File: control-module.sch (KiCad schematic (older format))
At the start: 19 parts

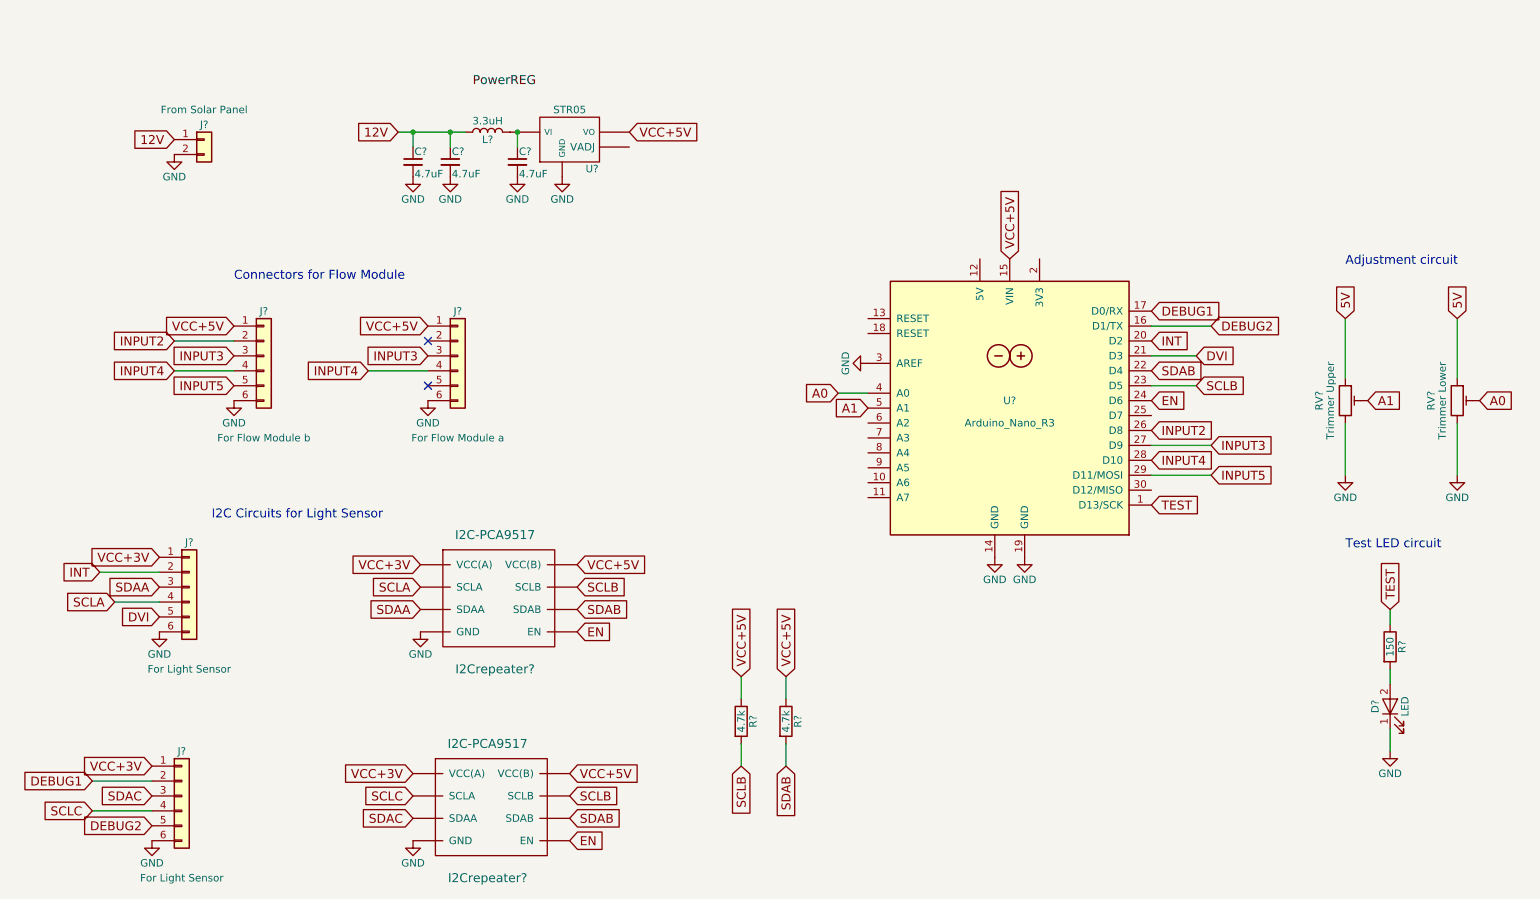
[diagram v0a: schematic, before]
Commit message: PCB Layout for Control Module
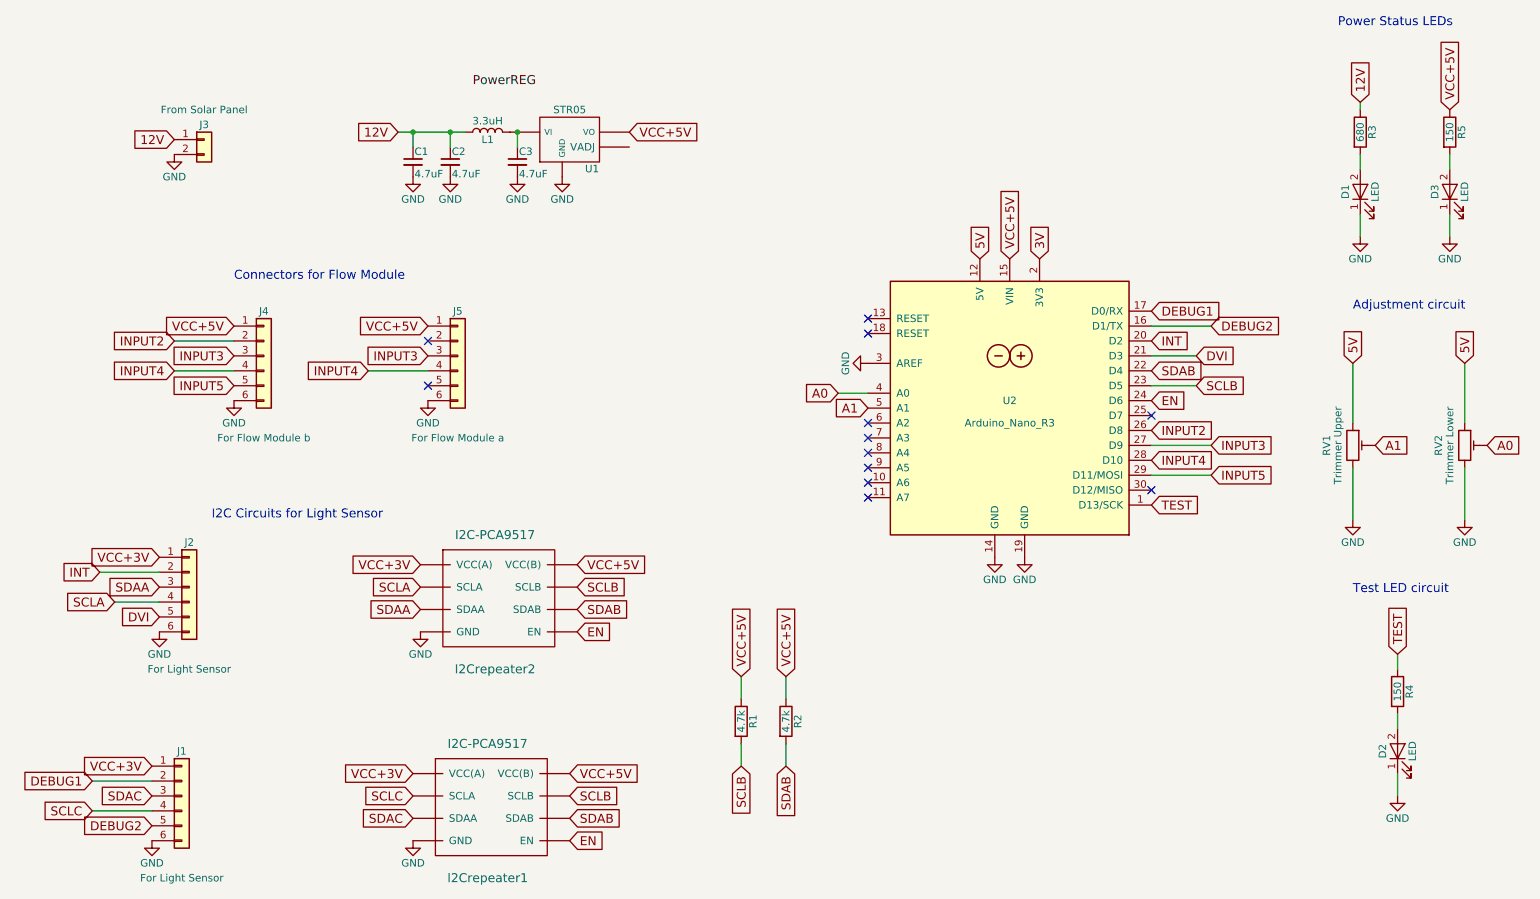
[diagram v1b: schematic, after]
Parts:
- removed C?: 4.7uF, symbol C_Small
- added C1: 4.7uF, Capacitors_SMD:C_0805_HandSoldering, symbol C_Small
- added D1, D3: LED, LEDs:LED_0805_HandSoldering, symbol LED
- added R3: 680, Resistors_SMD:R_0805_HandSoldering, symbol R
- added R5: 150, Resistors_SMD:R_0805_HandSoldering, symbol R
- C2, C3: renamed from C?; footprint (none) -> Capacitors_SMD:C_0805_HandSoldering
- D2: renamed from D?; footprint (none) -> LEDs:LED_0805_HandSoldering
- I2Crepeater1, I2Crepeater2: renamed from I2Crepeater?; footprint (none) -> Housings_SSOP:TSSOP-8_3x3mm_Pitch0.65mm
- J1, J2, J4, J5: renamed from J?; footprint (none) -> valveteam-footprints:Molex_KK-6410-06_06x2.54mm_Straight
- J3: renamed from J?; footprint (none) -> valveteam-footprints:TE_TERM
- L1: renamed from L?; footprint (none) -> valveteam-footprints:WURTH_INDUCTOR
- R1, R2, R4: renamed from R?; footprint (none) -> Resistors_SMD:R_0805_HandSoldering
- RV1, RV2: renamed from RV?; footprint (none) -> Potentiometers:Potentiometer_Trimmer_Vishay_T73XX_Vertical
- U1: renamed from U?; footprint (none) -> valveteam-footprints:STR05
- U2: renamed from U?; footprint (none) -> valveteam-footprints:Arduino_Nano
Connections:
- net 12V: now also C1.1, R3.1
- net 5V: now also U2.12 (5V)
- net GND: now also C1.2, D1.1 (K), D3.1 (K)
- net VCC+5V: now also R5.1
- net 3V: now reaches U2.2 (3V3)
- new net: D1.2 (A), R3.2
- new net: D3.2 (A), R5.2
- no-connect marks 2 -> 12
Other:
- note added: "Power Status LEDs"
- moved on the sheet: D2, R4, RV1, RV2
